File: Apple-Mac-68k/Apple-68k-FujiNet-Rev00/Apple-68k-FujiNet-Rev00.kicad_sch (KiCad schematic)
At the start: 26 parts, among them J1 Apple IDC-20, J2 Logic Analyzer, J3 UART, J4 SWD, P1 ST-TF-003A, SW1 ButtonA, SW2 Safe Reset, U1 Pico, U2 ESP32-S3-DevKitC-1 N16R8

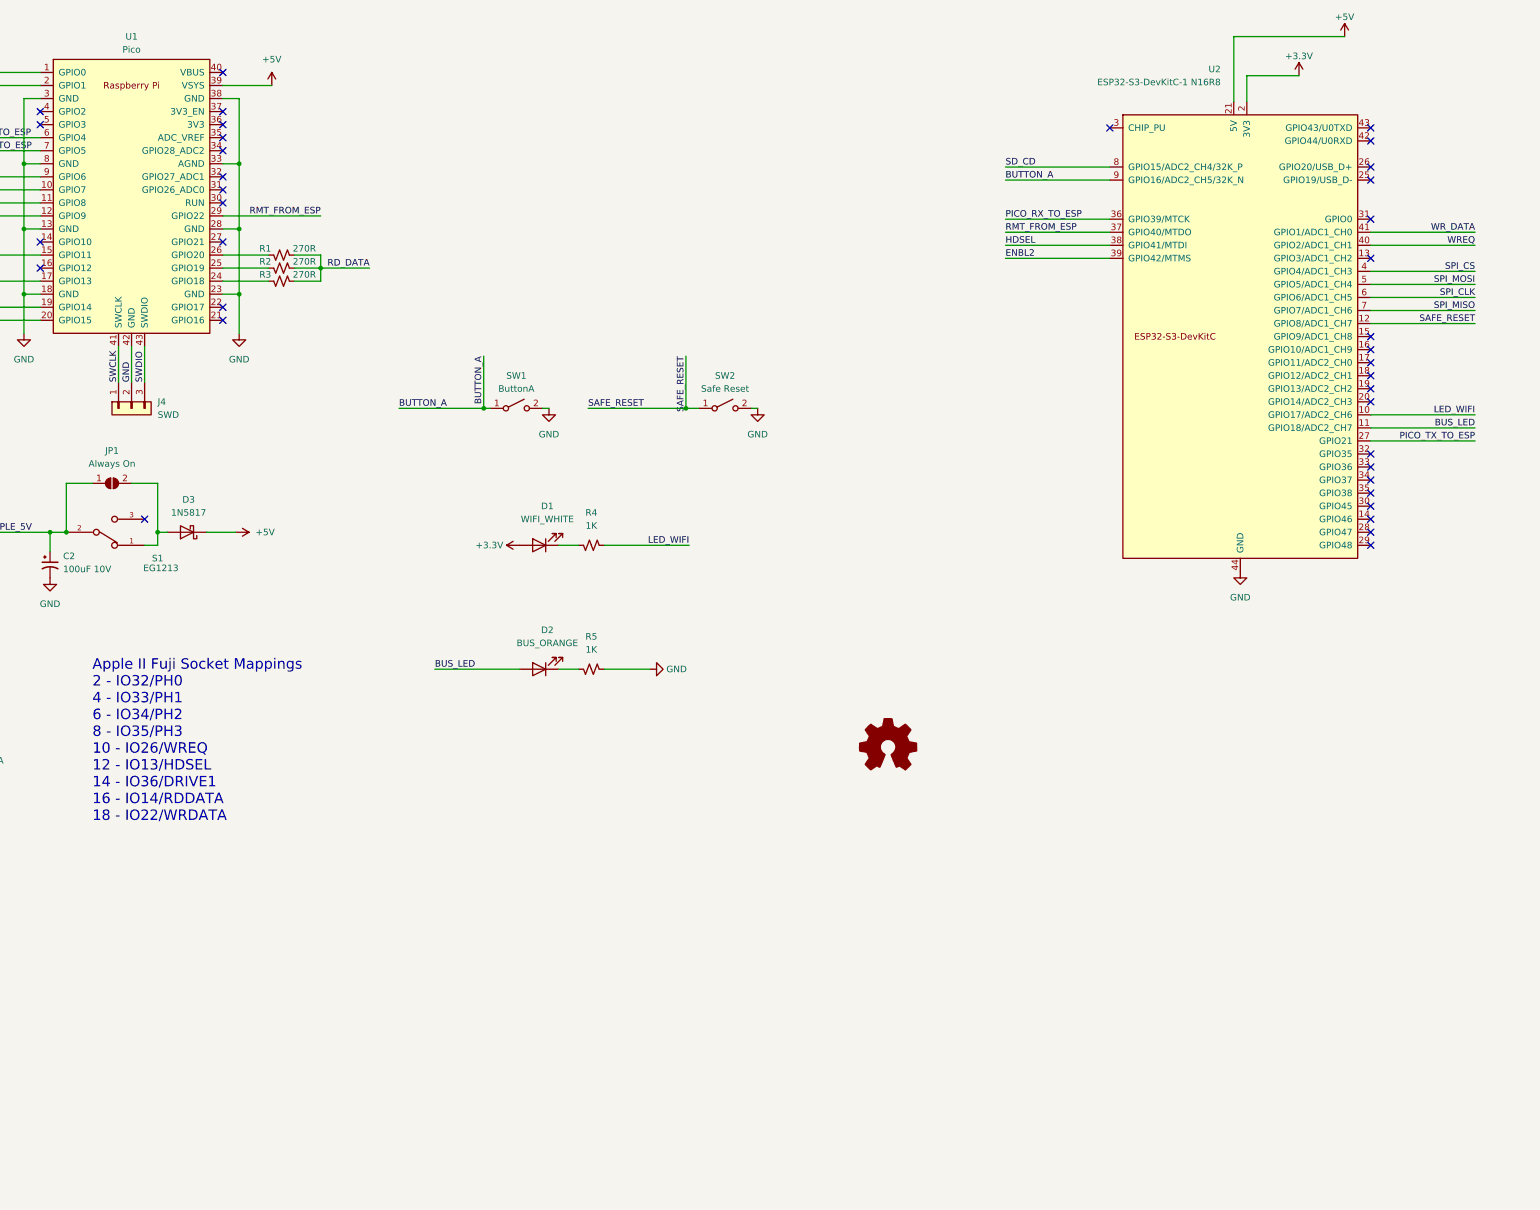
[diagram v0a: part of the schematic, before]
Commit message: Tidy Apple 68k Rev00 schematic layout
Move U2 back to the old ESP32 spot, the switch and LED groups to the
right, and the OSHW logo beside the title block. Drop the stale Apple II
socket mapping note.

Co-Authored-By: Claude Opus 5.5 <noreply@anthropic.com>
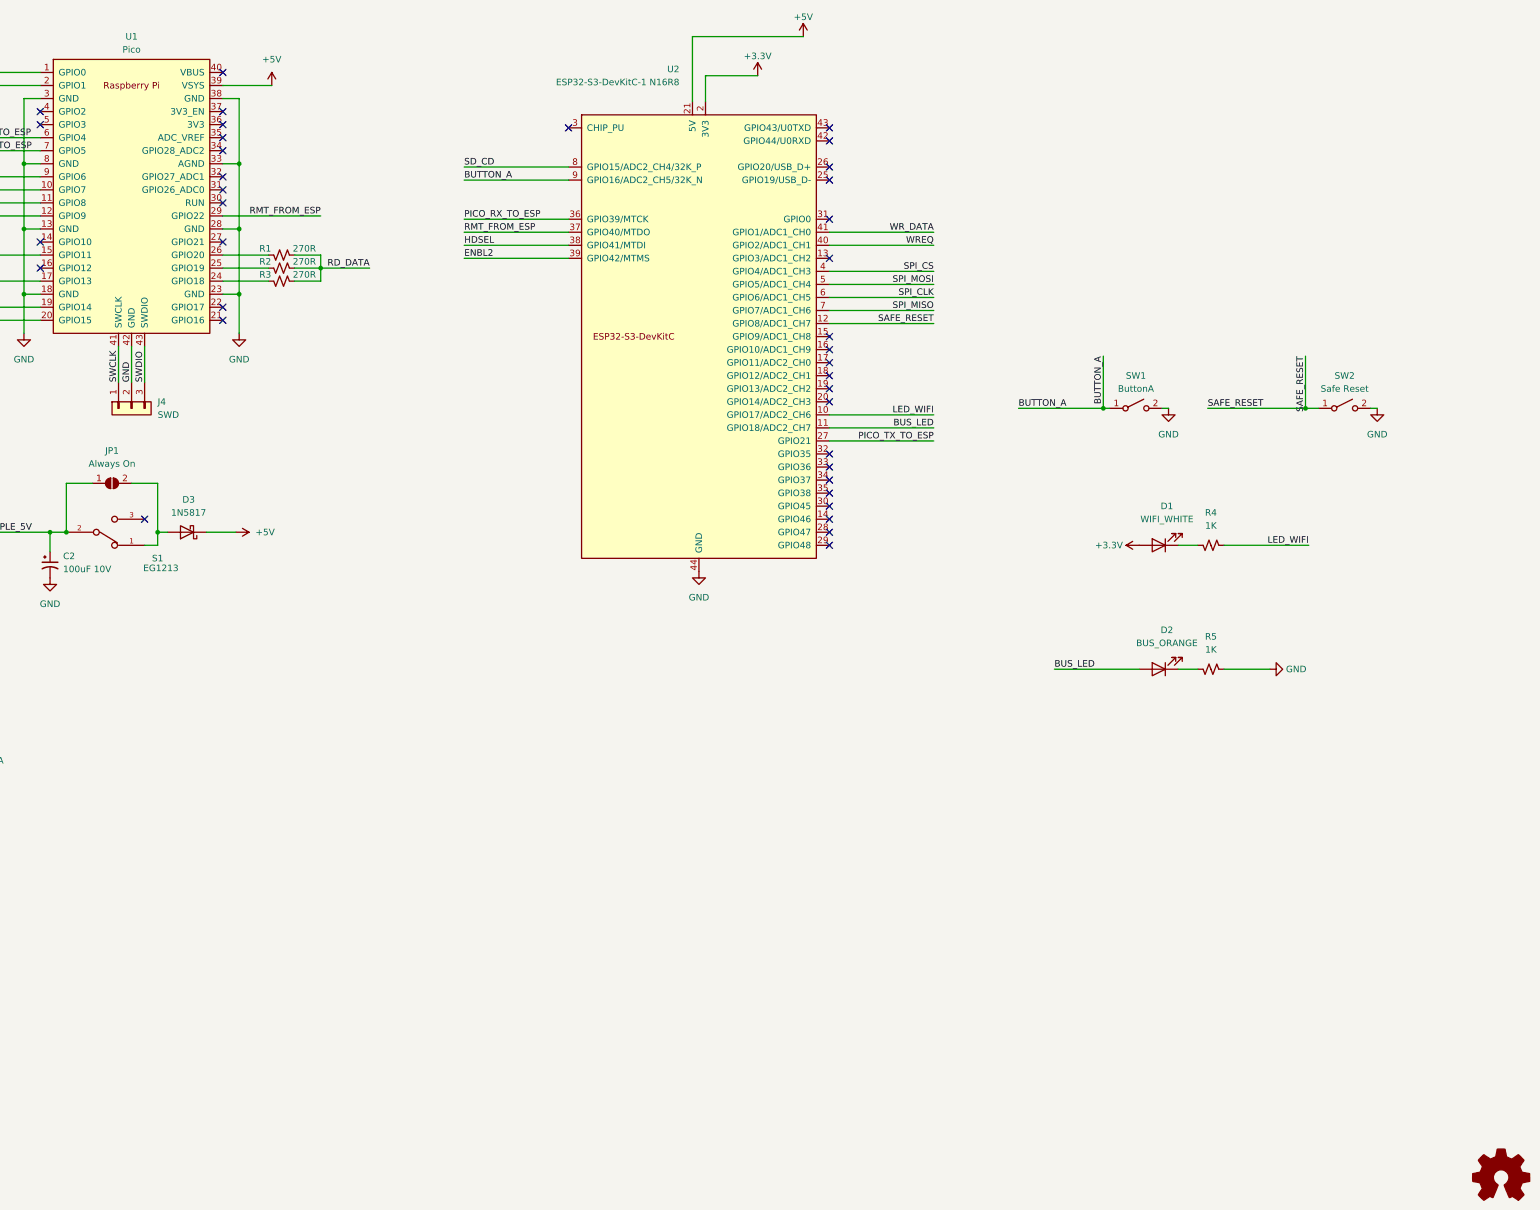
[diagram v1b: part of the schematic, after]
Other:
- note removed: "Apple II Fuji Socket Mappings 2 - IO32/PH0 4 - IO33/PH1 6 - IO34/PH2 8 - IO35/PH3 10 - IO26/WREQ 12 - IO13/HDSEL 14 - IO36/DRIVE1 16 - IO14/RDDATA 18 - IO22/WRDATA"
- moved on the sheet: D1, D2, R4, R5, SW1, SW2, U2
